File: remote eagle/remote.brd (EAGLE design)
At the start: 36.8 x 36.8 mm, 12 parts, among them U1 BLE112-A

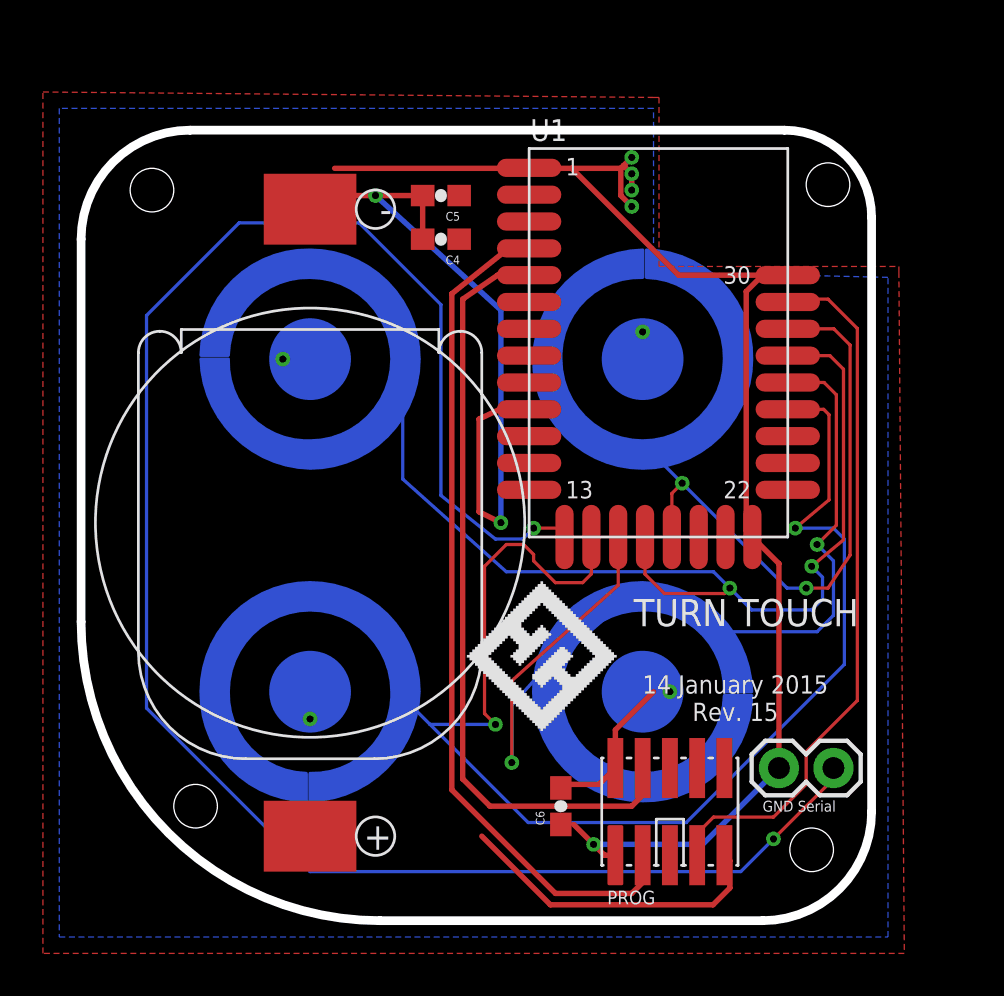
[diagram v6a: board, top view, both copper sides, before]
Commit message: Revision 15 of the board, with active LOW buttons, moved off P1_0/1.
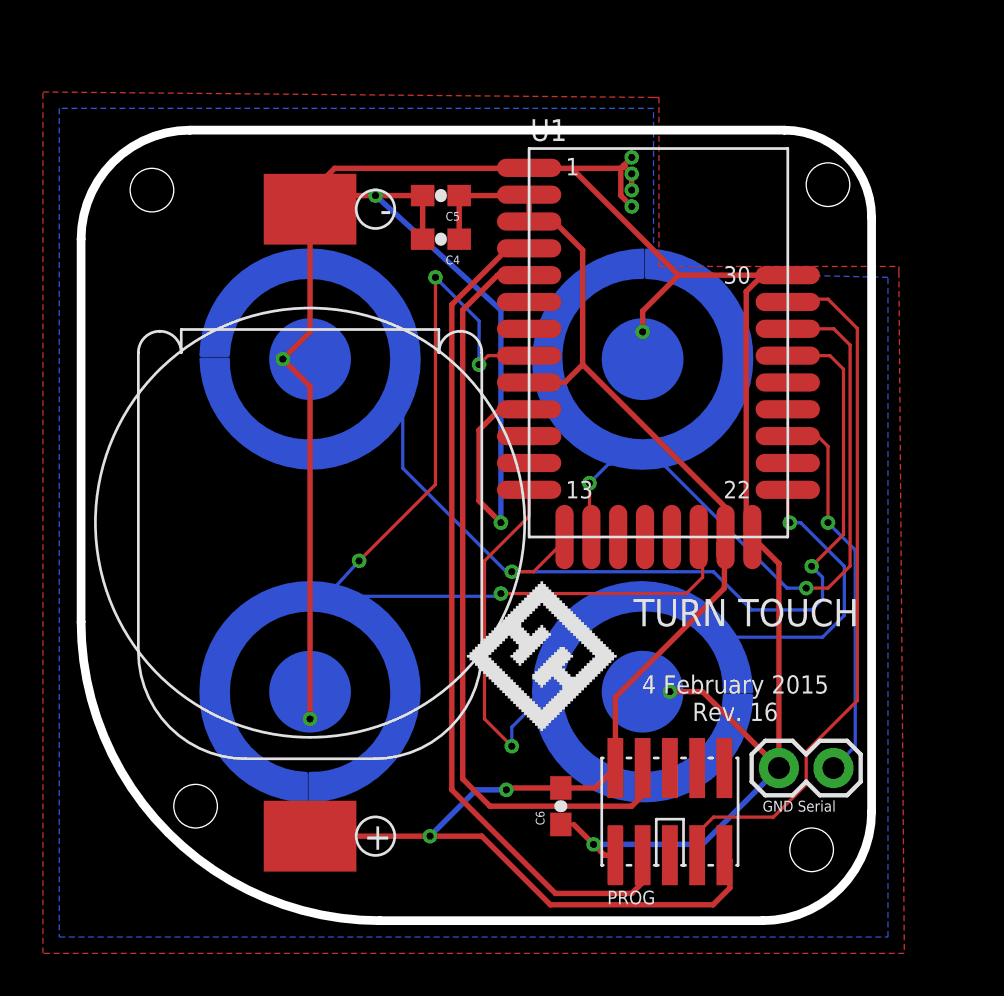
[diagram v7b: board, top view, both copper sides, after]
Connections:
- removed net P0_6: U1.P0_6
- removed net P0_7: U1.P0_7
- removed net P1_4: U1.P1_4
- removed net P1_5: U1.P1_5
- removed net P1_6: U1.P1_6
- new net P0_2: U1.P0_2
- new net P0_3: U1.P0_3
- new net P1_0: U1.P1_0
- new net P1_1: U1.P1_1
- new net P1_2: U1.P1_2
- net 3.3V: no longer U$1.P$1, U$1.P$2, U$2.P$1, U$2.P$2, U$3.P$1, U$3.P$2, U$4.P$1, U$4.P$2
- net BUTTON1: now also U1.P1_3; no longer U1.P1_0
- net BUTTON2: now also U1.P1_4; no longer U1.P1_1
- net BUTTON3: now also U1.P0_6, U1.P1_5; no longer U1.P0_2, U1.P1_2
- net BUTTON4: now also U1.P0_7, U1.P1_6; no longer U1.P0_3, U1.P1_3
- net GND: now also U$1.P$1, U$1.P$2, U$2.P$1, U$2.P$2, U$3.P$1, U$3.P$2, U$4.P$1, U$4.P$2
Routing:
- net SERIAL: track 88.0 -> 18.0 mm, vias 2 -> 1
- net 3.3V: track 22.0 -> 74.6 mm, vias 0 -> 2
- net GND: track 100.6 -> 143.6 mm
- net BUTTON4: track 69.0 -> 45.7 mm, vias 2 -> 4
- net BUTTON3: track 47.9 -> 41.2 mm
- net BUTTON1: track 28.7 -> 32.4 mm
- net BUTTON2: track 48.4 -> 46.0 mm
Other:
- board text added: "4 February 2015 Rev. 16"
- board text removed: "14 January 2015 Rev. 15"

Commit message: Remote pcb revision 17. Moving drill holes, embiggening caps.
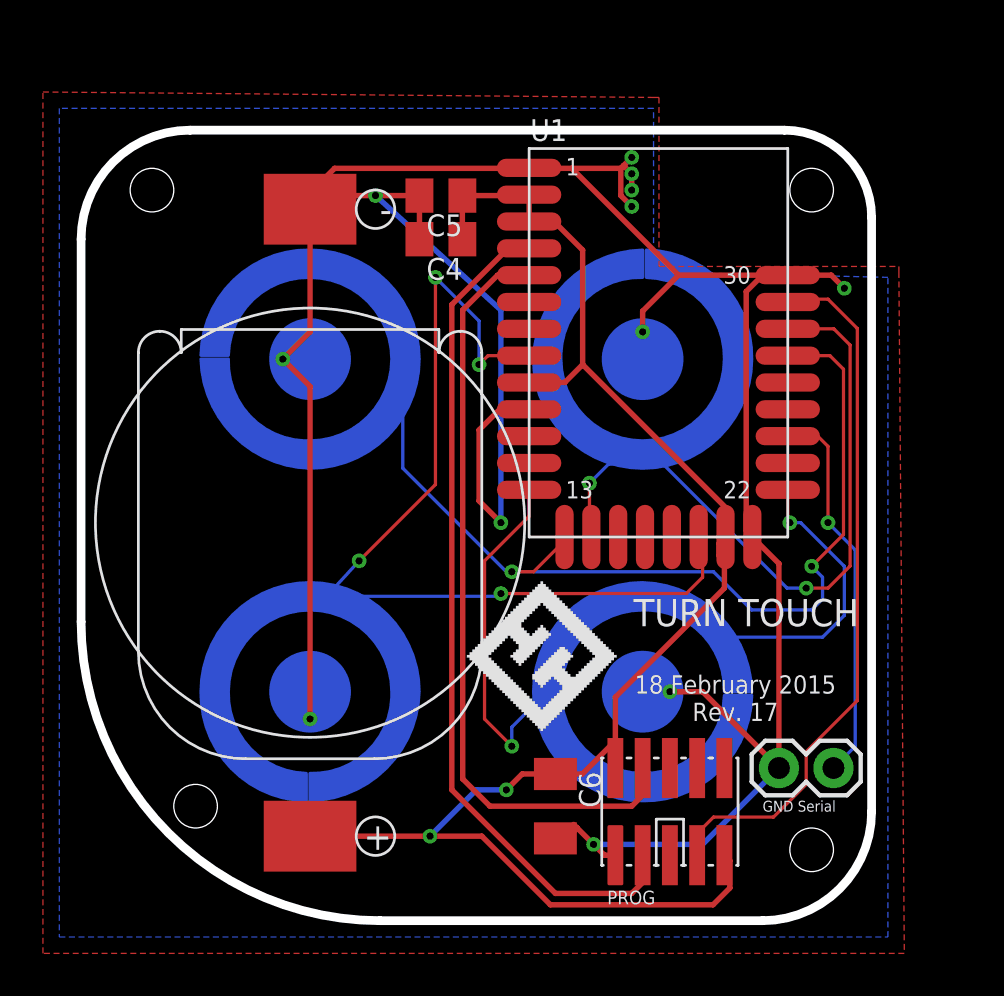
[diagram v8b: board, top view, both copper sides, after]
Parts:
- C4, C5: device SparkFun:0603-CAP -> resistor:C0805K
- C6: device SparkFun:0603-CAP -> resistor:C1206K
- moved C6 0.25 mm to (22.1, 5.33), turned to 270 degrees
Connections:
- net 3.3V: now also C6.1; no longer C6.2
- net GND: now also C6.2; no longer C6.1
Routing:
- net GND: track 143.6 -> 146.7 mm, vias 7 -> 8
- net 3.3V: track 74.6 -> 75.1 mm
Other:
- board text added: "18 February 2015 Rev. 17"
- board text removed: "4 February 2015 Rev. 16"
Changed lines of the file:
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@@
 <?xml version="1.0" encoding="utf-8"?>
 <!DOCTYPE eagle SYSTEM "eagle.dtd">
-<eagle version="7.0.0">
+<eagle version="7.2.0">
 <drawing>
 <settings>
@@
 <setting verticaltext="up"/>
 </settings>
-<grid distance="0.01" unitdist="inch" unit="inch" style="dots" multiple="1" display="yes" altdistance="0.005" altunitdist="inch" altunit="inch"/>
+<grid distance="0.01" unitdist="inch" unit="mm" style="dots" multiple="1" display="yes" altdistance="0.005" altunitdist="inch" altunit="inch"/>
 <layers>
 <layer number="1" name="Top" color="4" fill="1" visible="yes" active="yes"/>
@@
 <board>
 <plain>
-<text x="30.48" y="11.43" size="0.85" layer="25" font="vector" rot="SR0" align="top-center">4 February 2015
-Rev. 16</text>
+<text x="30.48" y="11.43" size="0.85" layer="25" font="vector" rot="SR0" align="top-center">18 February 2015
+Rev. 17</text>
 <text x="30.988" y="14.986" size="1.27" layer="25" font="vector" rot="SR0" align="top-center">TURN TOUCH</text>
 <text x="31.75" y="5.08" size="0.508" layer="25">GND Serial</text>
 <hole x="3.302" y="34.036" drill="2.032"/>
 <hole x="34.036" y="3.302" drill="2.032"/>
-<hole x="34.798" y="34.29" drill="2.032"/>
+<hole x="34.036" y="34.036" drill="2.032"/>
 <hole x="5.334" y="5.334" drill="2.032"/>
 <wire x1="0" y1="31.75" x2="0" y2="13.923740625" width="0.4064" layer="20"/>
@@
 </element>
 <element name="U1" library="sf-bluegiga" package="BLE112-A" value="BLE112-A" x="26.924" y="26.924"/>
-<element name="C4" library="SparkFun" package="0603-CAP" value="1uF" x="16.764" y="31.75" rot="R180"/>
-<element name="C5" library="SparkFun" package="0603-CAP" value="1uF" x="16.764" y="33.782" rot="R180"/>
-<element name="C6" library="SparkFun" package="0603-CAP" value="100uF" x="22.352" y="5.334" rot="R90"/>
+<element name="C4" library="resistor" package="C0805K" value="1uF" x="16.764" y="31.75" rot="R180"/>
+<element name="C5" library="resistor" package="C0805K" value="1uF" x="16.764" y="33.782" rot="R180"/>
+<element name="C6" library="resistor" package="C1206K" value="100uF" x="22.098" y="5.334" rot="R270"/>
 <element name="U$1" library="remote" package="DOME-M-SERIES" value="SNAPTRON-DOME" x="26.162" y="26.162" rot="MR0"/>
 <element name="U$2" library="remote" package="DOME-M-SERIES" value="SNAPTRON-DOME" x="10.668" y="26.162" rot="MR270"/>
@@
 <contactref element="C5" pad="2"/>
 <contactref element="C4" pad="2"/>
-<polygon width="0.4064" layer="16" pour="hatch">
+<polygon width="0.4064" layer="16" spacing="0.762" pour="hatch">
 <vertex x="-1.016" y="-0.762"/>
 <vertex x="37.592" y="-0.762"/>
@@
 <vertex x="-1.016" y="37.846"/>
 </polygon>
-<polygon width="0.4064" layer="1" pour="hatch">
+<polygon width="0.4064" layer="1" spacing="0.762" pour="hatch">
 <vertex x="-1.778" y="38.608"/>
 <vertex x="26.67" y="38.354"/>
@@
 <wire x1="30.988" y1="29.312" x2="30.988" y2="18.16" width="0.254" layer="1"/>
 <wire x1="30.988" y1="18.16" x2="31.274" y2="17.874" width="0.254" layer="1"/>
-<wire x1="22.948" y1="4.484" x2="23.876" y2="3.556" width="0.254" layer="1"/>
-<wire x1="15.914" y1="33.782" x2="15.914" y2="31.75" width="0.254" layer="1"/>
-<wire x1="15.914" y1="33.782" x2="13.716" y2="33.782" width="0.254" layer="1"/>
+<wire x1="22.948" y1="4.484" x2="23.114" y2="4.318" width="0.254" layer="1"/>
+<wire x1="23.114" y1="4.318" x2="23.876" y2="3.556" width="0.254" layer="1"/>
+<wire x1="15.764" y1="33.782" x2="15.764" y2="31.75" width="0.254" layer="1"/>
+<wire x1="15.764" y1="33.782" x2="13.716" y2="33.782" width="0.254" layer="1"/>
 <wire x1="13.716" y1="33.782" x2="10.541" y2="33.782" width="0.254" layer="1"/>
 <wire x1="32.924" y1="30.074" x2="31.75" y2="30.074" width="0.254" layer="1"/>
@@
 <wire x1="22.86" y1="35.052" x2="21.404" y2="35.052" width="0.254" layer="1"/>
 <wire x1="21.404" y1="35.052" x2="20.874" y2="35.074" width="0.254" layer="1"/>
-<wire x1="30.988" y1="29.312" x2="31.75" y2="30.074" width="0.254" layer="1"/>
 <wire x1="20.874" y1="23.824" x2="19.506" y2="23.824" width="0.254" layer="1"/>
 <wire x1="19.506" y1="23.824" x2="18.542" y2="22.86" width="0.254" layer="1"/>
@@
 <wire x1="25.654" y1="34.798" x2="25.273" y2="35.179" width="0.254" layer="1"/>
 <wire x1="25.654" y1="34.798" x2="25.654" y2="34.036" width="0.254" layer="1"/>
-<contactref element="U$6" pad="P$2"/>
-<contactref element="C6" pad="1"/>
 <contactref element="U$3" pad="P$2"/>
 <contactref element="U$3" pad="P$1"/>
@@
 <contactref element="U$4" pad="P$2"/>
 <contactref element="U$4" pad="P$1"/>
-<wire x1="22.948" y1="4.484" x2="22.352" y2="4.484" width="0.1524" layer="1"/>
 <wire x1="26.162" y1="10.668" x2="27.432" y2="10.668" width="0.254" layer="16"/>
-<wire x1="10.668" y1="33.147" x2="10.668" y2="33.909" width="0.254" layer="1"/>
-<wire x1="10.668" y1="33.909" x2="11.811" y2="35.052" width="0.254" layer="1"/>
-<wire x1="10.668" y1="33.147" x2="10.668" y2="33.655" width="0.254" layer="1"/>
+<wire x1="10.668" y1="33.909" x2="11.3665" y2="34.6075" width="0.254" layer="1"/>
+<wire x1="11.3665" y1="34.6075" x2="11.811" y2="35.052" width="0.254" layer="1"/>
 <wire x1="10.668" y1="33.655" x2="10.541" y2="33.782" width="0.254" layer="1"/>
-<wire x1="10.668" y1="33.147" x2="10.668" y2="27.432" width="0.254" layer="1"/>
 <wire x1="10.668" y1="27.432" x2="9.398" y2="26.162" width="0.254" layer="1"/>
 <wire x1="9.398" y1="26.162" x2="10.668" y2="26.162" width="0.254" layer="16"/>
@@
 <wire x1="26.162" y1="28.398" x2="27.838" y2="30.074" width="0.254" layer="1"/>
 <wire x1="26.162" y1="27.432" x2="26.162" y2="26.162" width="0.254" layer="16"/>
+<contactref element="C6" pad="2"/>
+<wire x1="22.098" y1="3.834" x2="22.098" y2="3.81" width="0.254" layer="1"/>
+<wire x1="22.098" y1="3.81" x2="22.606" y2="3.81" width="0.254" layer="1"/>
+<wire x1="22.606" y1="3.81" x2="23.114" y2="4.318" width="0.254" layer="1"/>
+<contactref element="U$6" pad="P$2"/>
+<wire x1="32.924" y1="30.074" x2="34.95" y2="30.074" width="0.254" layer="1"/>
+<wire x1="34.95" y1="30.074" x2="35.56" y2="29.464" width="0.254" layer="1"/>
+<via x="35.56" y="29.464" extent="1-16" drill="0.3302" diameter="0.3302"/>
+<wire x1="30.988" y1="29.312" x2="31.75" y2="30.074" width="0.254" layer="1"/>
+<wire x1="10.668" y1="33.147" x2="10.668" y2="33.909" width="0.254" layer="1"/>
+<wire x1="10.668" y1="33.147" x2="10.668" y2="27.432" width="0.254" layer="1"/>
+<wire x1="10.541" y1="33.782" x2="10.668" y2="33.909" width="0.254" layer="1"/>
 </signal>
 <signal name="N$1">
@@
 <contactref element="U1" pad="VDD_USB"/>
 <contactref element="U$6" pad="P$1"/>
-<contactref element="C6" pad="2"/>
 <contactref element="PROG" pad="2"/>
 <contactref element="PROG" pad="9"/>
@@
 <wire x1="30.226" y1="1.524" x2="30.226" y2="2.796" width="0.254" layer="1"/>
 <wire x1="30.226" y1="2.796" x2="29.972" y2="3.05" width="0.254" layer="1"/>
-<wire x1="24.892" y1="10.414" x2="24.892" y2="7.11" width="0.254" layer="1"/>
+<wire x1="24.892" y1="10.414" x2="24.892" y2="8.382" width="0.254" layer="1"/>
+<wire x1="24.892" y1="8.382" x2="24.892" y2="7.11" width="0.254" layer="1"/>
 <wire x1="16.256" y1="3.937" x2="18.669" y2="3.937" width="0.254" layer="1"/>
 <wire x1="24.892" y1="10.414" x2="29.972" y2="15.494" width="0.254" layer="1"/>
@@
 <wire x1="29.718" y1="17.018" x2="29.718" y2="17.568" width="0.254" layer="1"/>
 <wire x1="29.718" y1="17.568" x2="30.024" y2="17.874" width="0.254" layer="1"/>
-<wire x1="22.352" y1="6.184" x2="23.966" y2="6.184" width="0.254" layer="1"/>
-<wire x1="23.966" y1="6.184" x2="24.892" y2="7.11" width="0.254" layer="1"/>
-<wire x1="22.352" y1="6.184" x2="19.9" y2="6.184" width="0.254" layer="1"/>
 <wire x1="19.9" y1="6.184" x2="19.812" y2="6.096" width="0.254" layer="1"/>
 <via x="19.812" y="6.096" extent="1-16" drill="0.3302"/>
@@
 <via x="16.256" y="3.937" extent="1-16" drill="0.3302"/>
 <wire x1="16.256" y1="3.937" x2="10.668" y2="3.937" width="0.254" layer="1"/>
-<wire x1="17.614" y1="31.75" x2="17.614" y2="33.782" width="0.254" layer="1"/>
-<wire x1="17.614" y1="33.782" x2="20.832" y2="33.782" width="0.254" layer="1"/>
+<wire x1="17.764" y1="31.75" x2="17.764" y2="33.782" width="0.254" layer="1"/>
+<wire x1="17.764" y1="33.782" x2="20.832" y2="33.782" width="0.254" layer="1"/>
 <wire x1="20.832" y1="33.782" x2="20.874" y2="33.824" width="0.254" layer="1"/>
 <wire x1="20.874" y1="33.824" x2="20.874" y2="32.574" width="0.254" layer="1"/>
@@
 <wire x1="30.024" y1="17.874" x2="30.024" y2="19.252" width="0.254" layer="1"/>
 <wire x1="30.024" y1="19.252" x2="23.368" y2="25.908" width="0.254" layer="1"/>
+<contactref element="C6" pad="1"/>
+<wire x1="22.098" y1="6.834" x2="23.344" y2="6.834" width="0.254" layer="1"/>
+<wire x1="23.344" y1="6.834" x2="24.892" y2="8.382" width="0.254" layer="1"/>
+<wire x1="22.098" y1="6.834" x2="20.55" y2="6.834" width="0.254" layer="1"/>
+<wire x1="20.55" y1="6.834" x2="19.812" y2="6.096" width="0.254" layer="1"/>
 </signal>
 <signal name="P0_2">
